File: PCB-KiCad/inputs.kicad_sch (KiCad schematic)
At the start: 11 parts, among them SW1 SW_DPDT_x2, SW2 SW_DPDT_x2, SW3 SW_DPDT_x2, SW4 SW_DPDT_x2, SW5 SW_DPDT_x2, U5 ATtiny84A-P, U6 74HC165, U7 74HC165

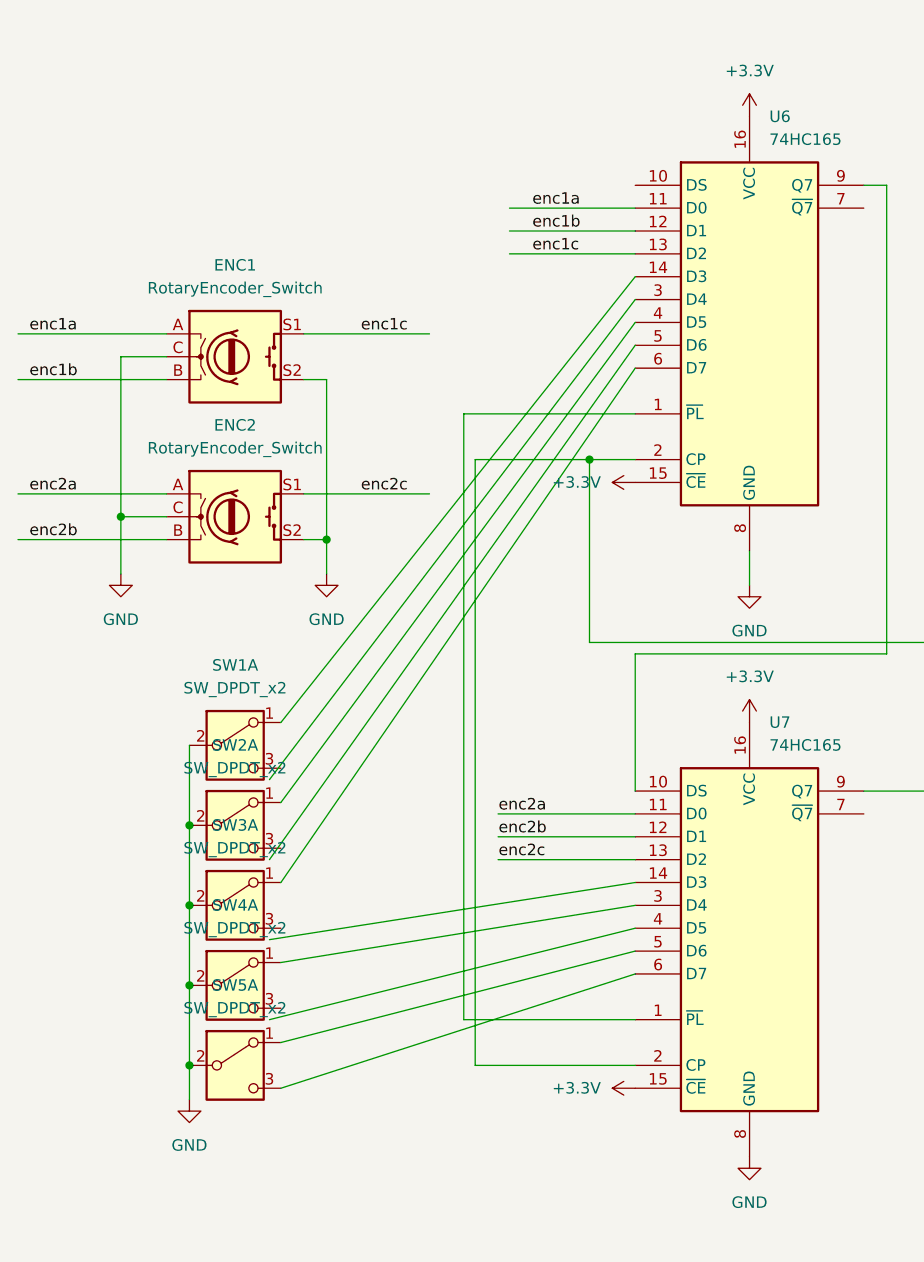
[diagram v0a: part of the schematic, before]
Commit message: GP1294 evolves
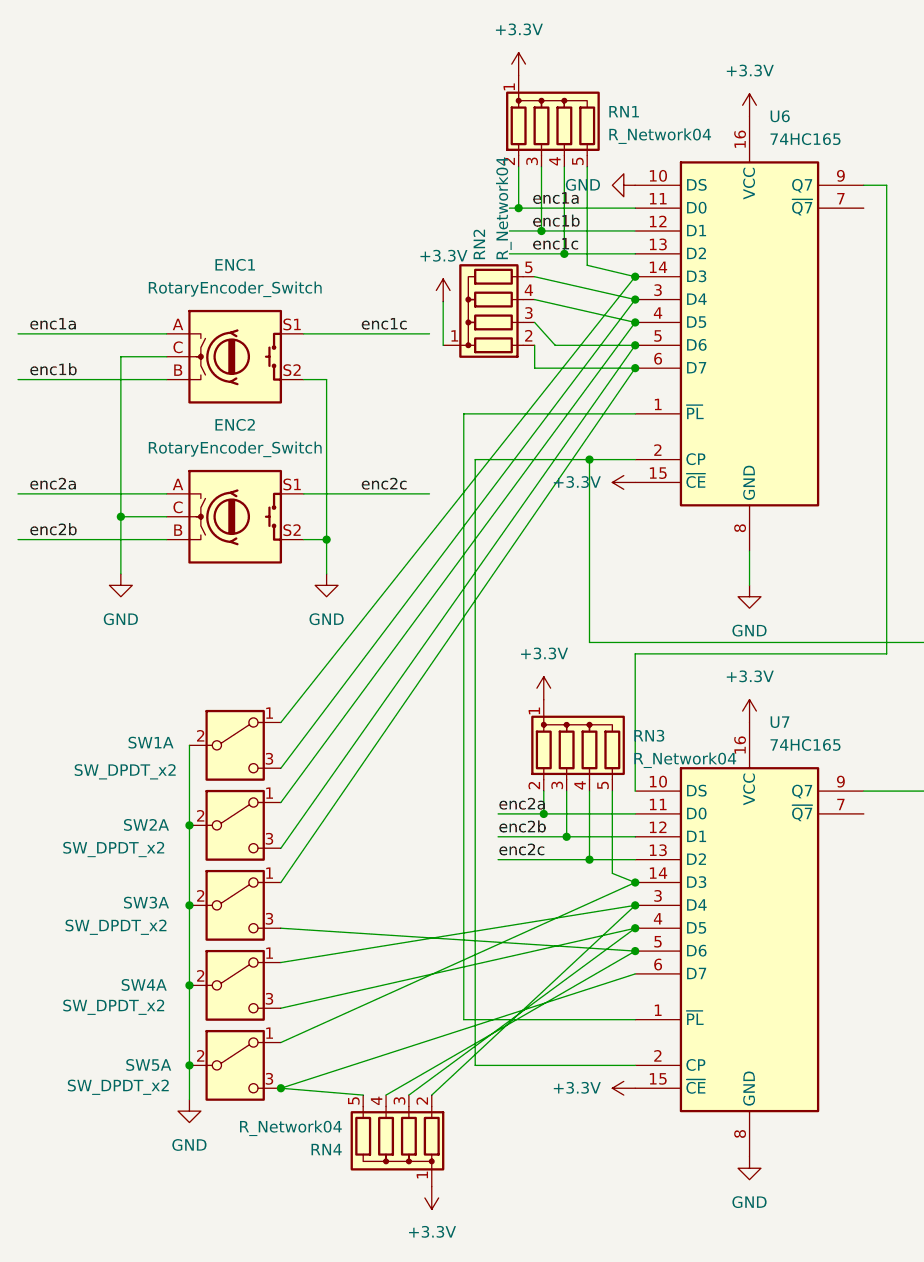
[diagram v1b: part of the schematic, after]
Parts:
- added RN1, RN2, RN3, RN4: R_Network04, Resistor_THT:R_Array_SIP5, symbol Device:R_Network04
- R10: footprint Resistor_SMD:R_0603_1608Metric -> Resistor_SMD:R_1206_3216Metric_Pad1.30x1.75mm_HandSolder
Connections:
- net +3.3V: now also RN1.1 (common), RN2.1 (common), RN3.1 (common), RN4.1 (common)
- net GND: now also U6.10 (DS)
- net enc1a: now also RN1.2 (R1)
- net enc1b: now also RN1.3 (R2)
- net enc1c: now also RN1.4 (R3)
- net enc2a: now also RN3.2 (R1)
- net enc2b: now also RN3.3 (R2)
- net enc2c: now also RN3.4 (R3)
- net at SW4.1 (A), U7.3 (D4): now also RN4.2 (R1)
- net at SW4.3 (C): now also U7.4 (D5), RN4.3 (R2)
- net at U7.14 (D3): now also SW5.1 (A), RN3.5 (R4)
- net at U7.5 (D6): now also SW3.3 (C), RN4.4 (R3); no longer SW5.1 (A)
- net at SW5.3 (C), U7.6 (D7): now also RN4.5 (R4)
- net at SW3.1 (A), U6.6 (D7): now also RN2.2 (R1)
- net at SW2.1 (A), U6.4 (D5): now also RN2.4 (R3)
- net at SW2.3 (C): now also U6.5 (D6), RN2.3 (R2)
- net at SW1.1 (A), U6.14 (D3): now also RN1.5 (R4)
- net at SW1.3 (C): now also U6.3 (D4), RN2.5 (R4)

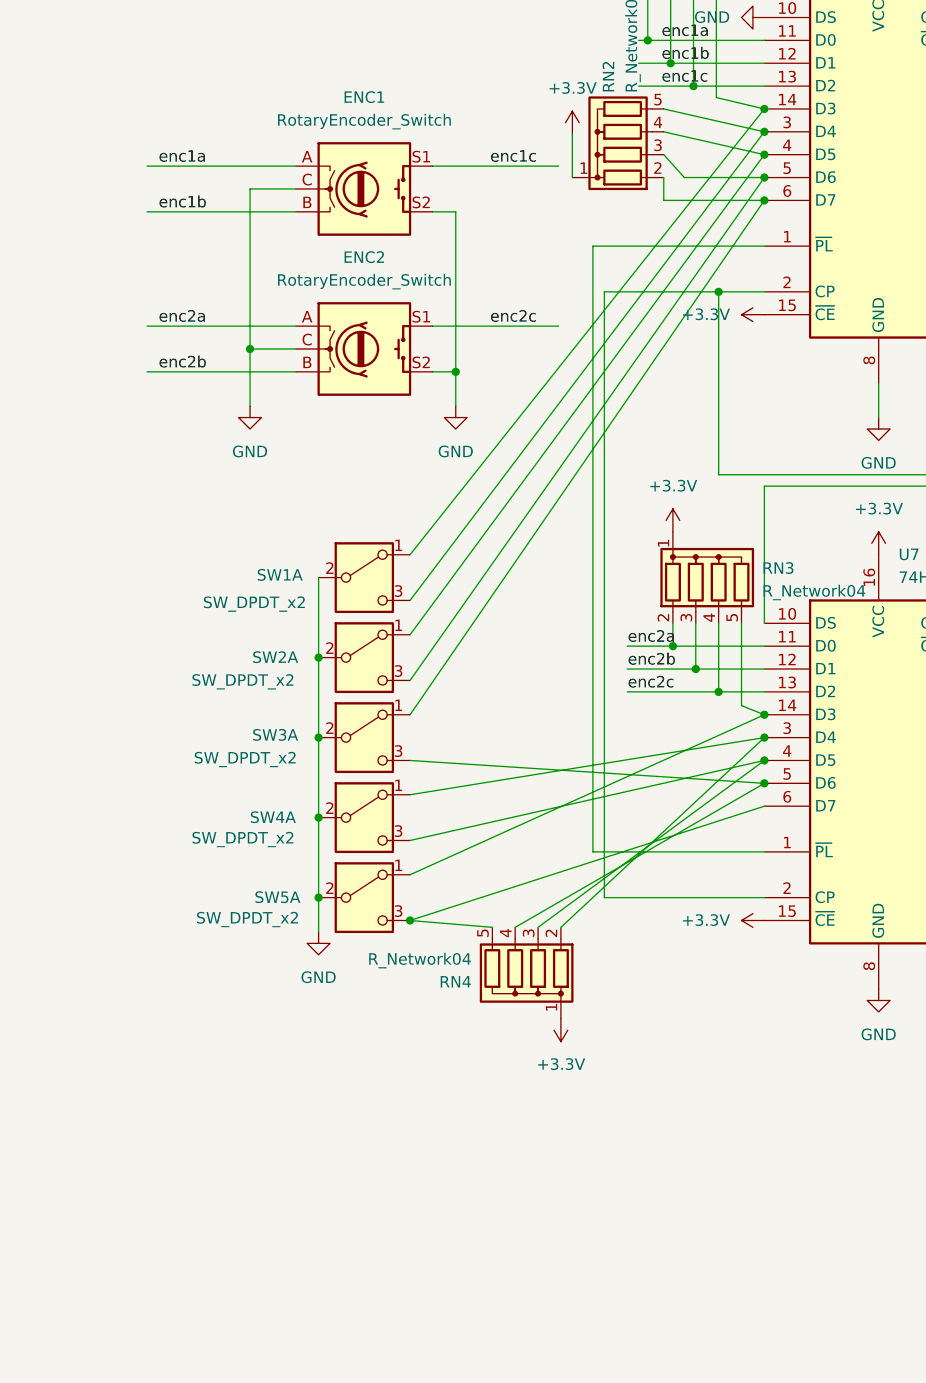
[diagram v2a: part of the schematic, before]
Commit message: Added Debounce Caps and stuff.
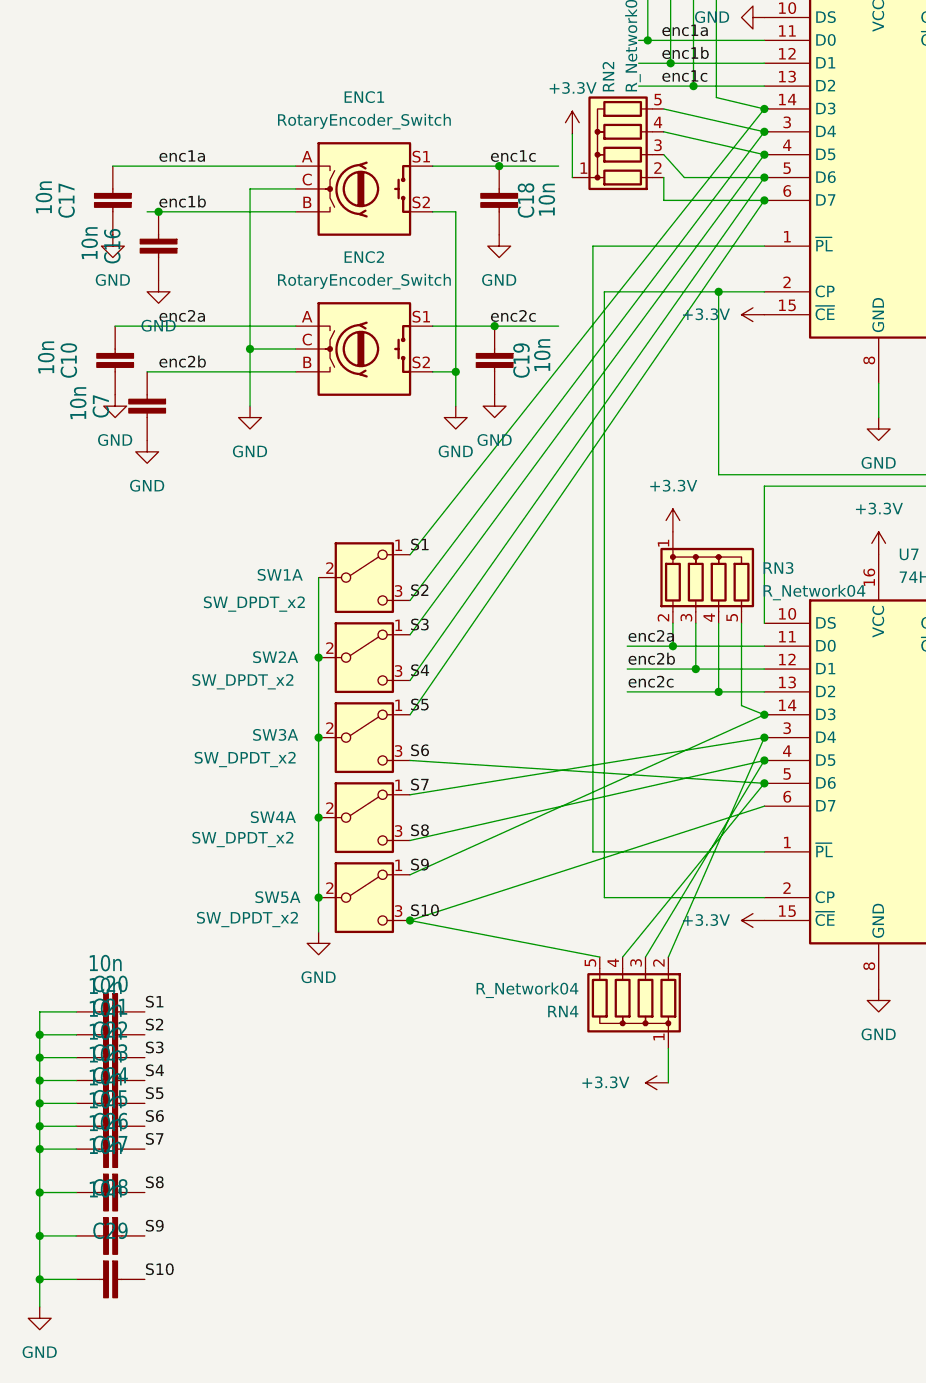
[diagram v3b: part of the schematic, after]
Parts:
- added C10, C16, C17, C18, C19, C20, C21, C22, C23, C24, C25, C26, C27, C28, C29, C7: 10n, VFD-Power:C1206, symbol VFD-Power:C-EUC1206
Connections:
- net GND: now also C10.1, C16.1, C17.1, C18.1, C19.1, C20.2, C21.2, C22.2, C23.2, C24.2, C25.2, C26.2, C27.2, C28.2, C29.2, C7.1
- net enc1a: now also C17.2
- net enc1b: now also C16.2
- net enc1c: now also C18.2
- net enc2a: now also C10.2
- net enc2b: now also C7.2
- net enc2c: now also C19.2
- net S7: now reaches RN4.2 (R1), SW4.1 (A), U7.3 (D4)
- net S7: now also C26.1
- net S8: now reaches RN4.3 (R2), SW4.3 (C), U7.4 (D5)
- net S8: now also C27.1
- net S6: now reaches RN4.4 (R3), SW3.3 (C), U7.5 (D6)
- net S6: now also C25.1
- net S10: now reaches RN4.5 (R4), SW5.3 (C), U7.6 (D7)
- net S10: now also C29.1
- net S9: now reaches RN3.5 (R4), SW5.1 (A), U7.14 (D3)
- net S9: now also C28.1
- net S5: now reaches RN2.2 (R1), SW3.1 (A), U6.6 (D7)
- net S5: now also C24.1
- net S3: now reaches RN2.4 (R3), SW2.1 (A), U6.4 (D5)
- net S3: now also C22.1
- net S4: now reaches RN2.3 (R2), SW2.3 (C), U6.5 (D6)
- net S4: now also C23.1
- net S1: now reaches RN1.5 (R4), SW1.1 (A), U6.14 (D3)
- net S1: now also C20.1
- net S2: now reaches RN2.5 (R4), SW1.3 (C), U6.3 (D4)
- net S2: now also C21.1
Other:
- moved on the sheet: RN4

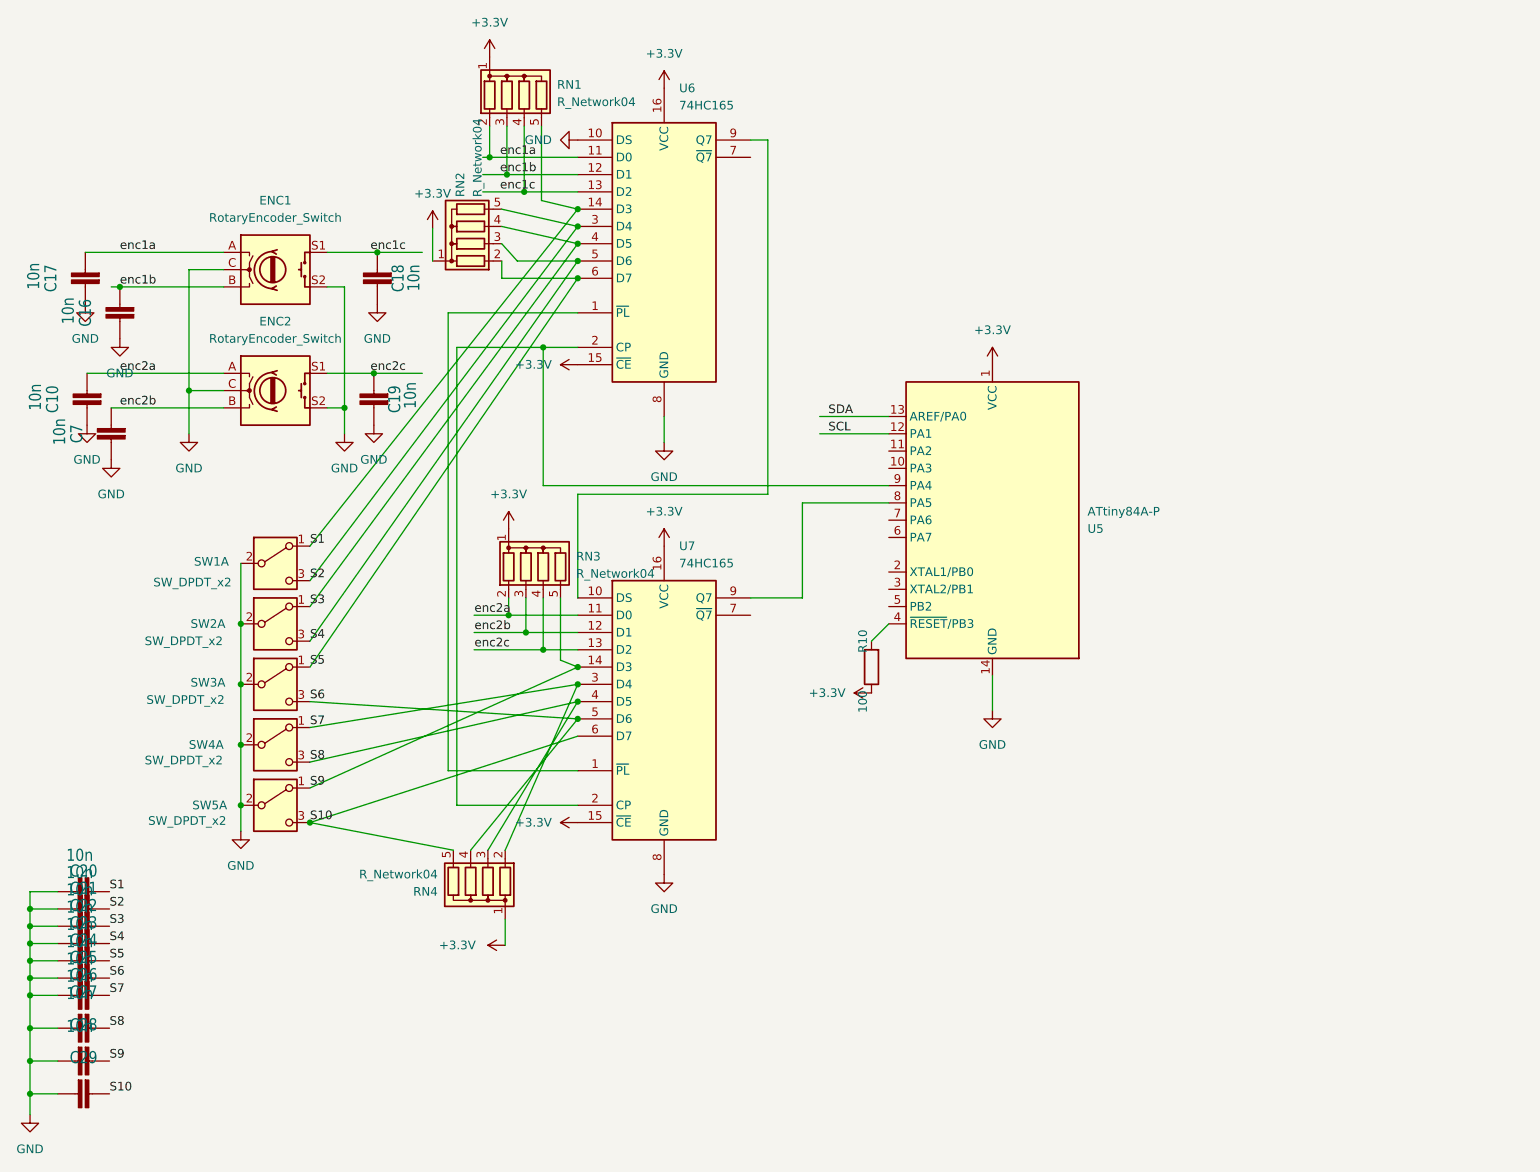
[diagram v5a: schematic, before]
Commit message: Fixed i2c..
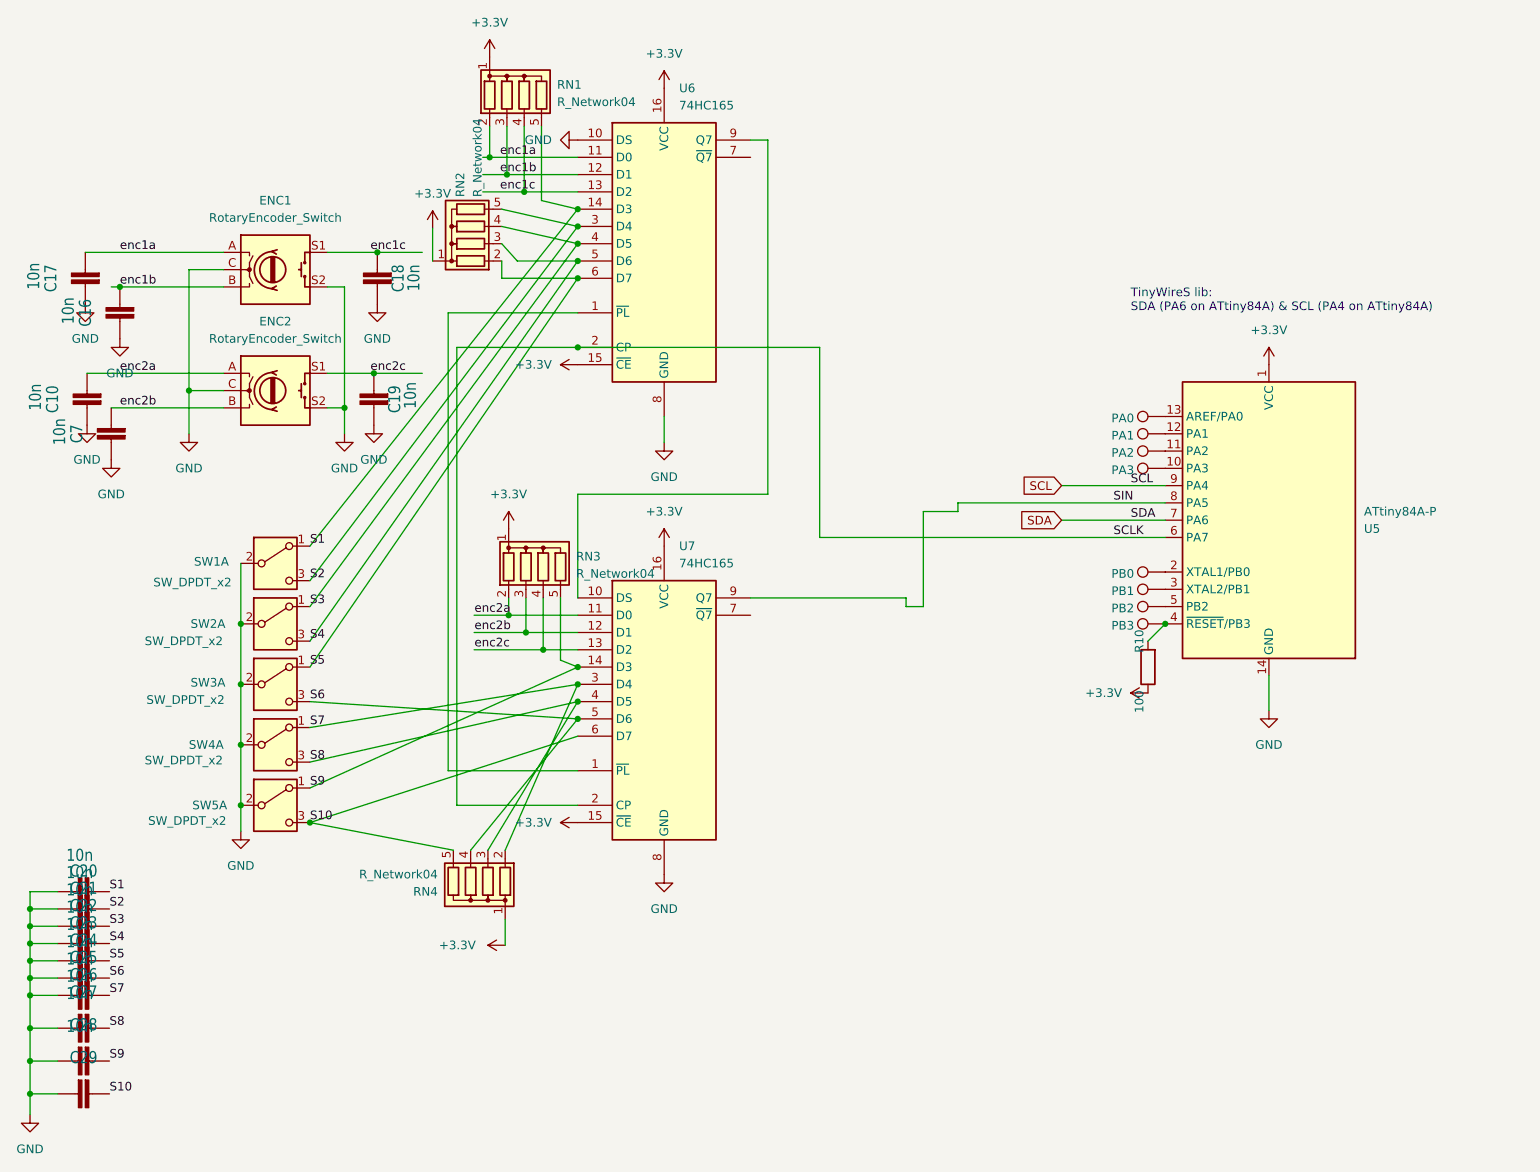
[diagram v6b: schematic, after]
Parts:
- added TP17: PB3, TestPoint:TestPoint_Pad_2.0x2.0mm, symbol Connector:TestPoint
- added TP18: PB2, TestPoint:TestPoint_Pad_2.0x2.0mm, symbol Connector:TestPoint
- added TP19: PB1, TestPoint:TestPoint_Pad_2.0x2.0mm, symbol Connector:TestPoint
- added TP20: PB0, TestPoint:TestPoint_Pad_2.0x2.0mm, symbol Connector:TestPoint
- added TP21: PA3, TestPoint:TestPoint_Pad_2.0x2.0mm, symbol Connector:TestPoint
- added TP22: PA2, TestPoint:TestPoint_Pad_2.0x2.0mm, symbol Connector:TestPoint
- added TP23: PA1, TestPoint:TestPoint_Pad_2.0x2.0mm, symbol Connector:TestPoint
- added TP24: PA0, TestPoint:TestPoint_Pad_2.0x2.0mm, symbol Connector:TestPoint
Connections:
- net SCL: now also U5.9 (PA4); no longer U5.12 (PA1)
- net SDA: now also U5.7 (PA6); no longer U5.13 (AREF/PA0)
- net at R10.2, U5.4 (~{RESET}/PB3): now also TP17.1
- net SCLK: now reaches U6.2 (CP), U7.2 (CP)
- net SCLK: now also U5.6 (PA7); no longer U5.9 (PA4)
- net SIN: now reaches U5.8 (PA5), U7.9 (Q7)
- net at U5.10 (PA3): now also TP21.1
- net at U5.11 (PA2): now also TP22.1
- net at U5.2 (XTAL1/PB0): now also TP20.1
- net at U5.3 (XTAL2/PB1): now also TP19.1
- net at U5.5 (PB2): now also TP18.1
- new net: TP23.1, U5.12 (PA1)
- new net: TP24.1, U5.13 (AREF/PA0)
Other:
- note added: "TinyWireS lib: SDA (PA6 on ATtiny84A) & SCL (PA4 on ATtiny84A)"
- moved on the sheet: R10, U5
